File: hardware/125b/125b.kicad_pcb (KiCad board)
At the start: 2 copper layers, 59 x 75 mm, 52 parts, among them J1 Guitar in, J2 Barrel_Jack, J3 Conn_02x05_Odd_Even_MountingP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, J4 NRJ6HF, SW1 SW_DIP_x02, SW2 RotaryEncoder_Switch, SW3 Switch 1, SW4 Switch 2, U1 L78L05_TO92, U2 TL074

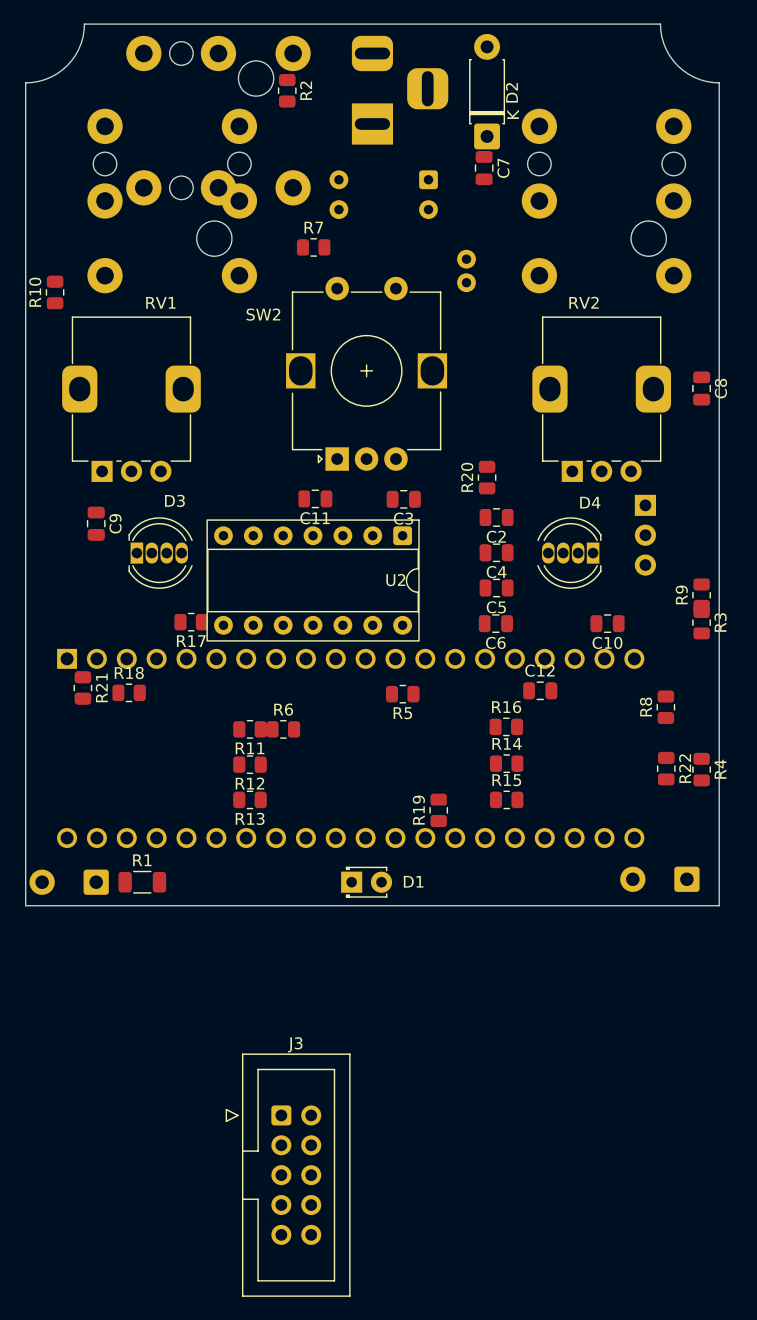
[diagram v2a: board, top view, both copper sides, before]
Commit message: Update 3d models and adjust footprints for local project lib
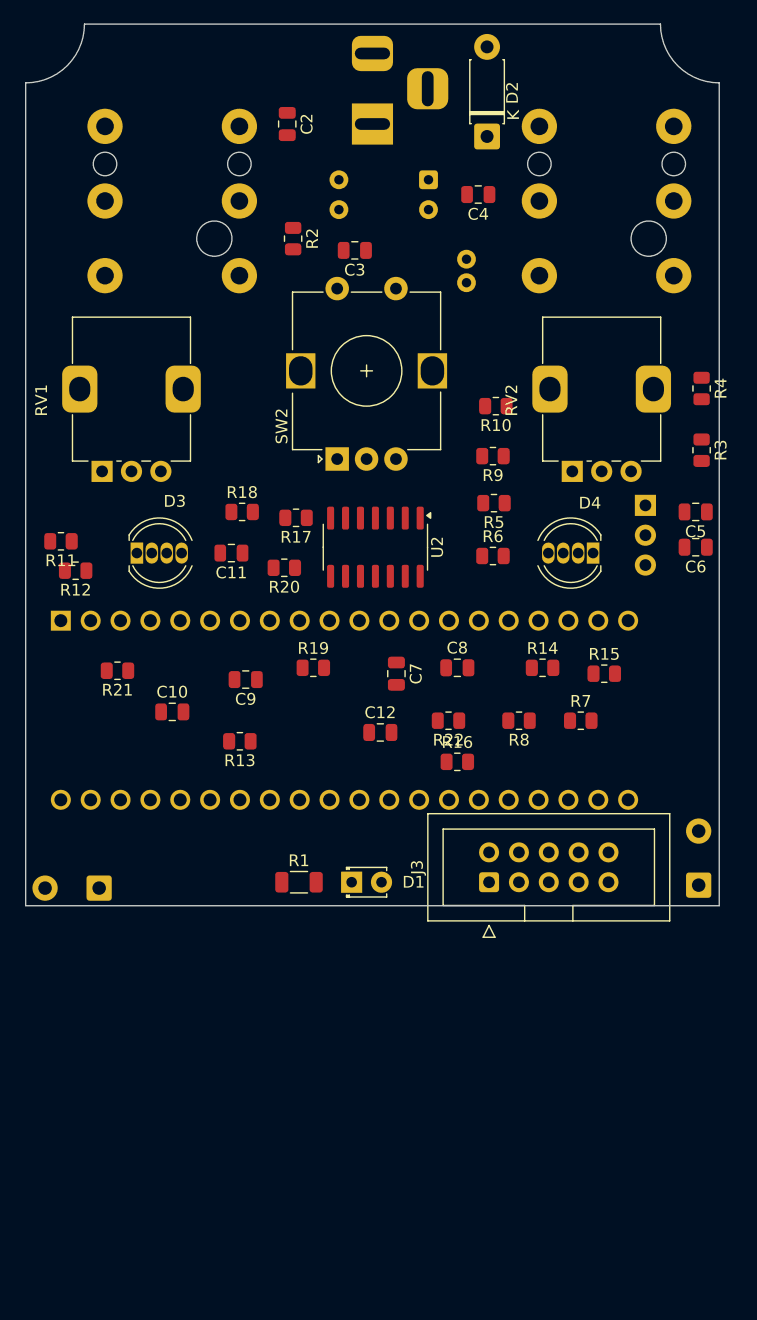
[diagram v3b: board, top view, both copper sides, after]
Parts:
- removed the J4 at (120.8, 37.5)
- A1: footprint Module:Electrosmith_Daisy_Seed -> Library:Electrosmith_Daisy_Seed
- J1: footprint Connector_Audio:Jack_6.35mm_Neutrik_NRJ6HF-1-AU_Horizontal -> Library:Jack_6.35mm_Neutrik_NRJ6HF-1-AU_Horizontal
- J4: value NRJ6HF -> Guitar out; footprint Connector_Audio:Jack_6.35mm_Neutrik_NRJ6HF_Horizontal -> Library:Jack_6.35mm_Neutrik_NRJ6HF-1-AU_Horizontal
- RV1, RV2: footprint Potentiometer_THT:Potentiometer_Alps_RK09K_Single_Vertical -> Project:Potentiometer_Alps_RK09K_Single_Vertical
- SW2: footprint Rotary_Encoder:RotaryEncoder_Alps_EC12E-Switch_Vertical_H20mm -> Project:RotaryEncoder_Alps_EC12E-Switch_Vertical_H20mm
- U2: footprint Package_DIP:DIP-14_W7.62mm_Socket -> Package_SO:SOIC-14_3.9x8.7mm_P1.27mm
- moved R7 46.2 mm to (145.2, 94.3)
- moved C7 43.7 mm to (129.5, 90.3)
- moved R10 38.7 mm to (138.0, 67.5), turned to 180 degrees
- moved C2 37.9 mm to (120.2, 43.5), turned to -90 degrees
- moved C10 37.8 mm to (110.5, 93.5), turned to 0 degrees
- moved R4 32.4 mm to (155.5, 66.0)
- moved C8 31.6 mm to (134.7, 89.8), turned to 0 degrees
- moved C4 30.5 mm to (136.5, 49.5)
- moved J3 26.6 mm to (137.4, 108.0), turned to 90 degrees
- moved R6 23.1 mm to (137.8, 80.2)
- moved R11 22.7 mm to (101.0, 79.0)
- moved R12 22.2 mm to (102.2, 81.5)
- moved C3 21.6 mm to (126.0, 54.2)
- moved R9 21.3 mm to (137.8, 71.8), turned to 180 degrees
- moved R22 19.0 mm to (134.0, 94.3), turned to 180 degrees
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
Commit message: Tidy up position of SMD components
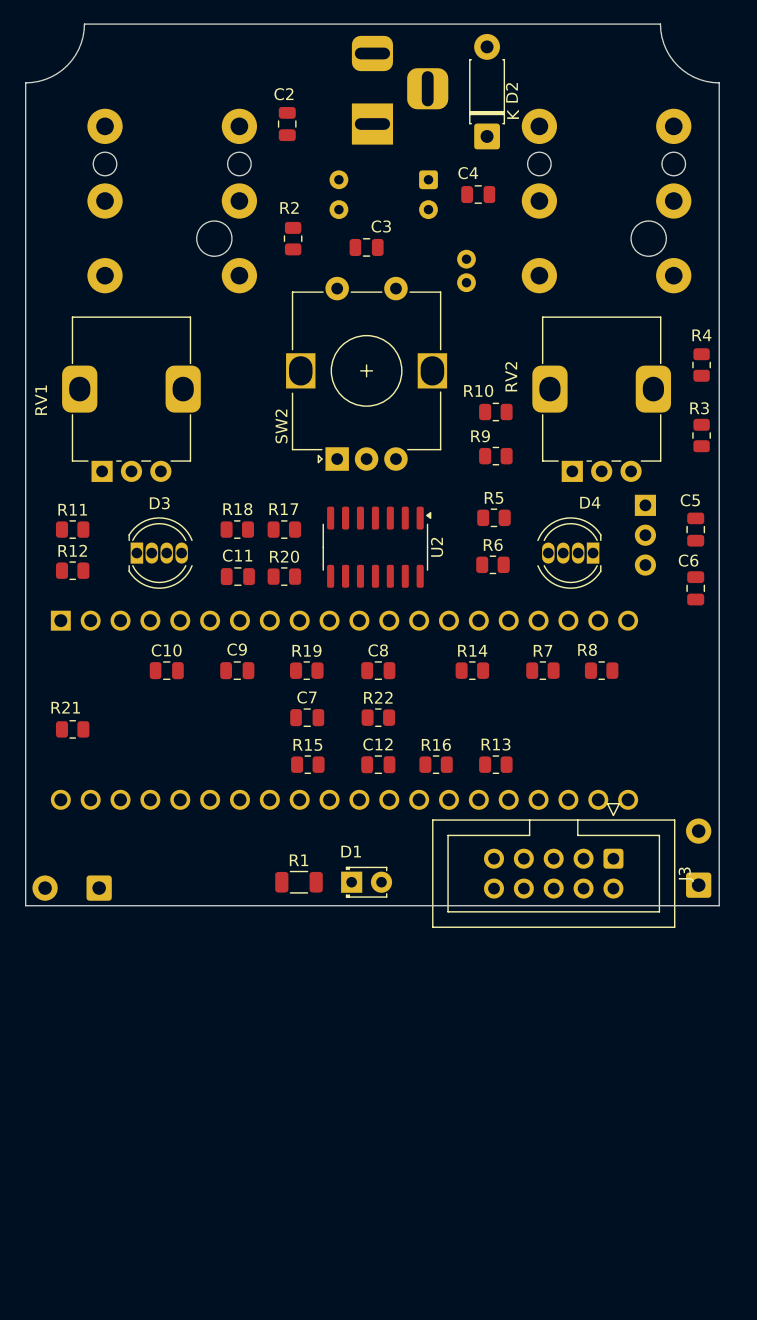
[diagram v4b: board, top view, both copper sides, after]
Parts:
- moved R15 26.4 mm to (122.0, 98.0)
- moved R13 21.9 mm to (138.0, 98.0)
- moved J3 10.8 mm to (148.0, 106.0), turned to -90 degrees
- moved C7 8.46 mm to (122.0, 94.0), turned to 0 degrees
- moved R8 8.22 mm to (147.0, 90.0)
- moved C8 6.72 mm to (128.0, 90.0)
- moved R21 6.28 mm to (102.0, 95.0)
- moved R22 5.98 mm to (128.0, 94.0), turned to 0 degrees
- moved R14 5.97 mm to (136.0, 90.0)
- moved R7 5.34 mm to (142.0, 90.0)
- moved C10 3.54 mm to (110.0, 90.0)
- moved C6 3.50 mm to (155.0, 83.0), turned to -90 degrees
- moved C12 2.75 mm to (128.0, 98.0)
- moved C11 2.07 mm to (116.0, 82.0)
- moved R4 2.00 mm to (155.5, 64.0), turned to 90 degrees
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
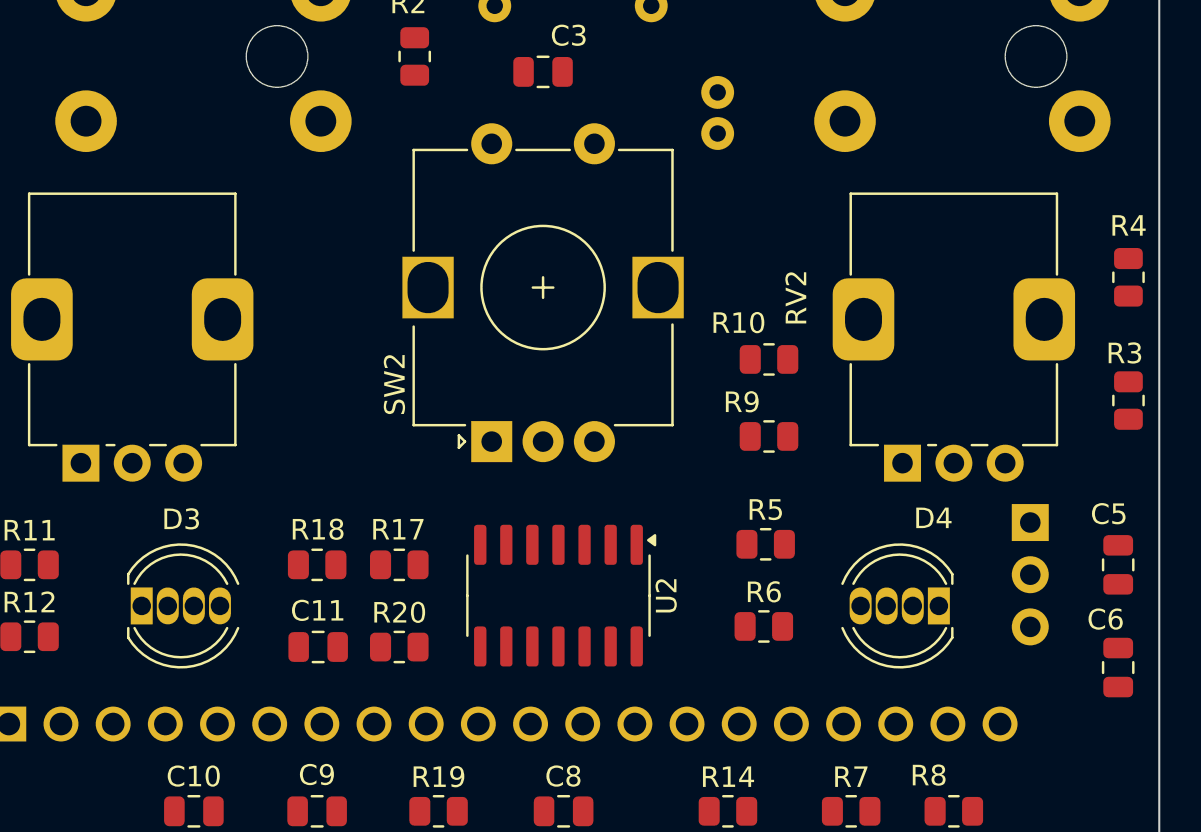
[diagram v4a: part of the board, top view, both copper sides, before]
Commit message: Increase RGB LED footprint for easier soldering
Also re-adjustLEDs, pots and encoder for symmetry
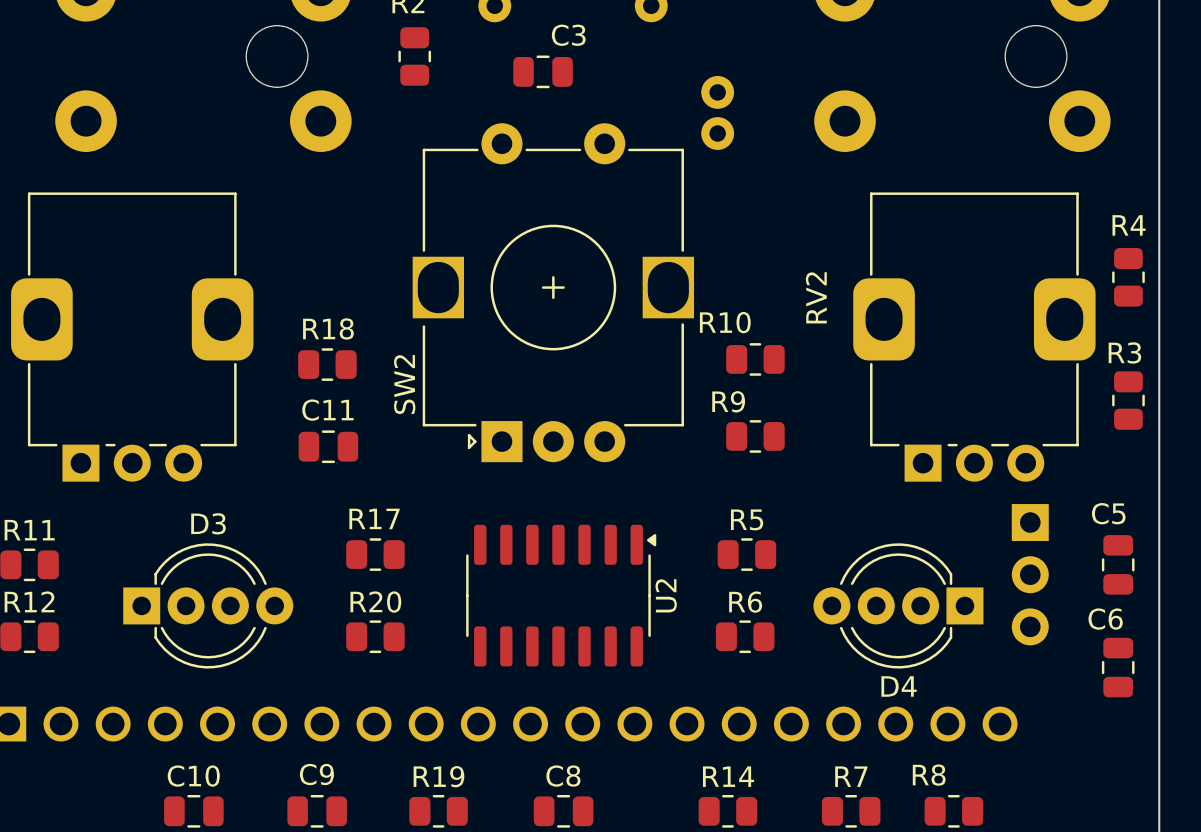
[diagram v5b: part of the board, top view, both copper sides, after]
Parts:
- D3, D4: footprint LED_THT:LED_D5.0mm-4_RGB -> LED_THT:LED_D5.0mm-4_RGB_Wide_Pins
- moved C11 9.76 mm to (116.5, 72.2)
- moved R18 9.76 mm to (116.5, 68.2)
- moved D4 1.27 mm to (147.5, 80.0)
- moved R17 1.27 mm to (118.8, 77.5)
- moved R20 1.27 mm to (118.8, 81.5)
- moved R5 1.04 mm to (136.9, 77.5)
- moved R6 1.04 mm to (136.8, 81.5)
- moved RV2 1.00 mm to (145.5, 73.0)
- moved R10 0.66 mm to (137.3, 68.0)
- moved R9 0.66 mm to (137.3, 71.8)
- moved SW2 0.50 mm to (125.0, 72.0)

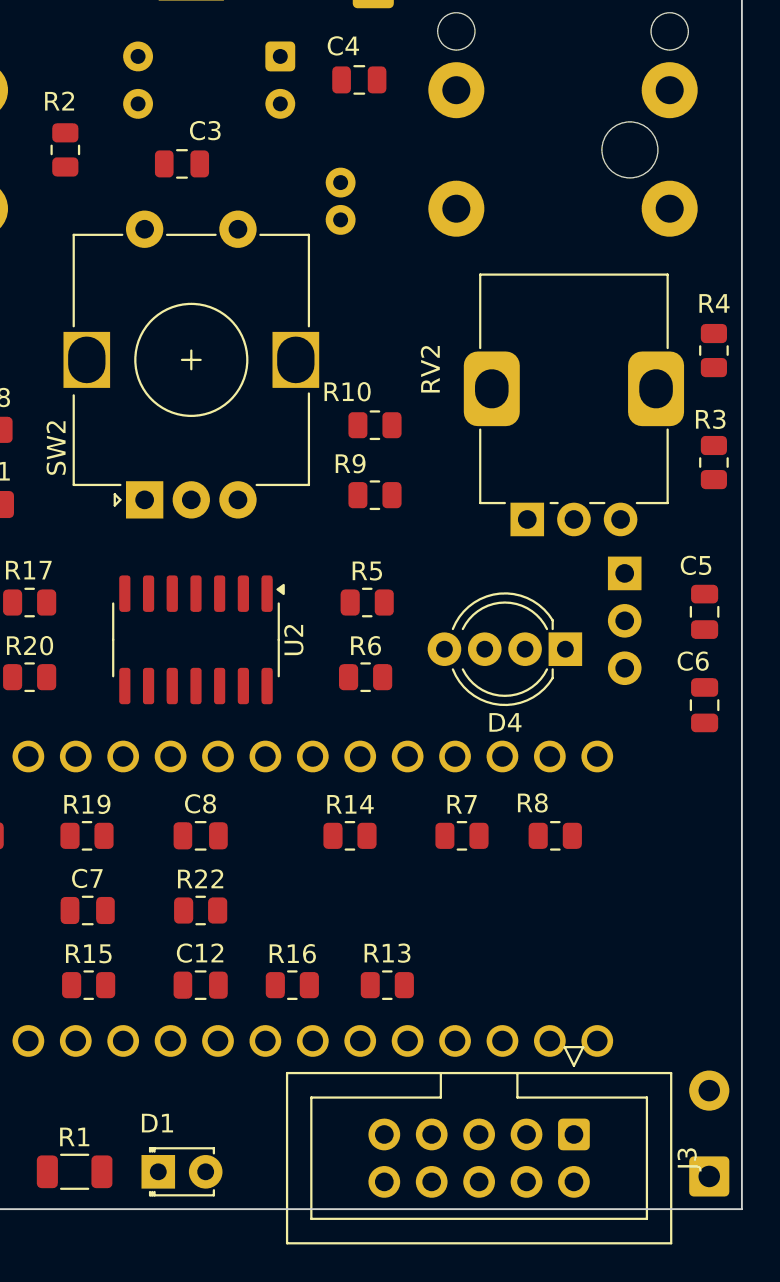
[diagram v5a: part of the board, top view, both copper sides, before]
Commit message: Try pin sockets for the footswitch connector
Can just solder some ribbon wire for this version
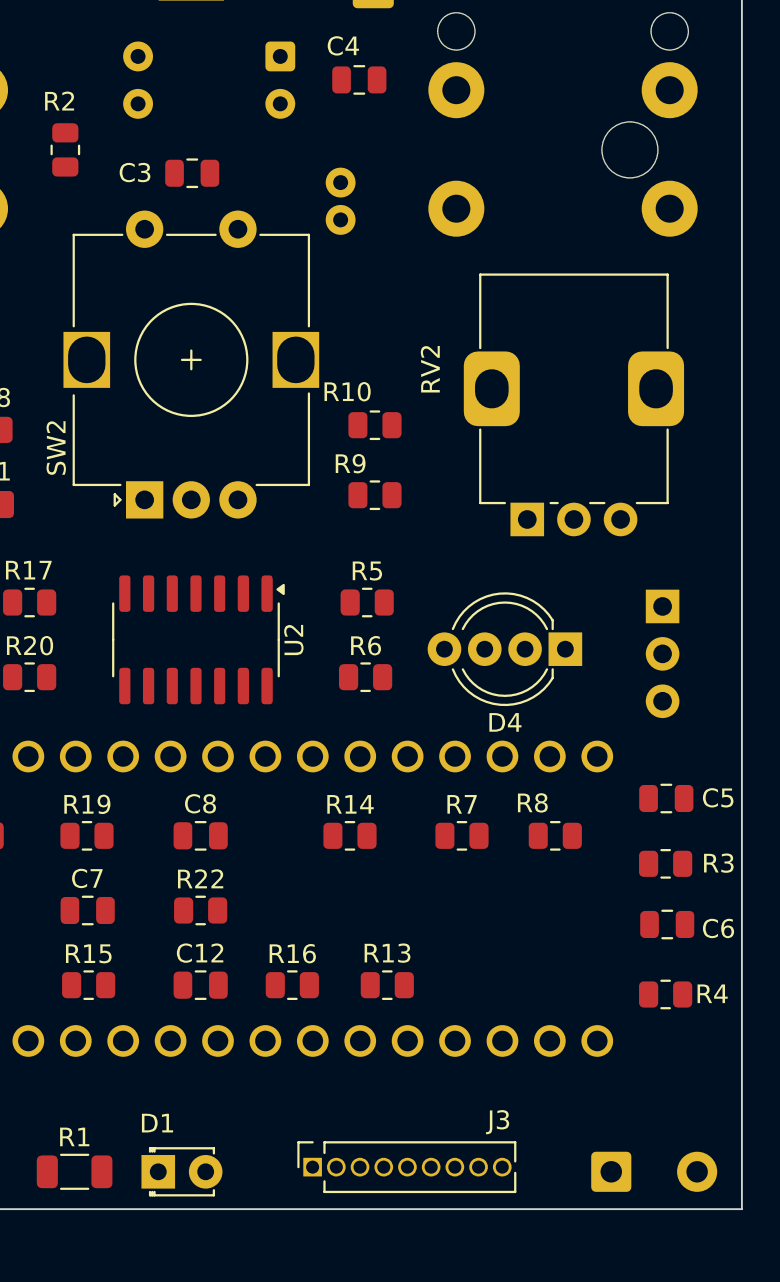
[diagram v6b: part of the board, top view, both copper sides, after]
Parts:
- J3: footprint Connector_IDC:IDC-Header_2x05_P2.54mm_Vertical -> Connector_PinSocket_1.27mm:PinSocket_1x09_P1.27mm_Vertical
- moved R4 34.6 mm to (152.9, 98.5), turned to 0 degrees
- moved R3 21.7 mm to (152.9, 91.5), turned to 180 degrees
- moved J3 14.1 mm to (134.0, 107.8), turned to 90 degrees
- moved C6 11.9 mm to (153.0, 94.8), turned to 180 degrees
- moved C5 10.2 mm to (152.9, 88.0), turned to 180 degrees
- moved SW4 5.26 mm to (150.0, 108.0), turned to 0 degrees
- moved U1 2.69 mm to (152.8, 77.7)
- moved C3 0.74 mm to (127.5, 54.5)

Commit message: Add GND plane zones
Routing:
- added copper zone on B.Cu, net GND
- added copper zone on F.Cu, net GND
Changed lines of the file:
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@@
+		)
+	)
+	(zone
+		(net 20)
+		(net_name "GND")
+		(layers "F.Cu" "B.Cu")
+		(hatch edge 0.5)
+		(connect_pads
+			(clearance 0.4)
+		)
+		(min_thickness 0.25)
+		(filled_areas_thickness no)
+		(fill
+			(thermal_gap 0.5)
+			(thermal_bridge_width 0.5)
+		)
+		(polygon
+			(pts
+				(xy 150 35.75) (xy 156.5 42.25) (xy 156.5 109.25) (xy 156.25 109.5) (xy 98.5 109.5) (xy 98.5 42)
+				(xy 104.75 35.75)
+			)
 		)
 	)

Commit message: Everything connected together
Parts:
- C5, R20, R5, R6, R9, U2: moved to B.Cu
- moved R3 65.6 mm to (109.8, 42.0)
- moved R4 60.2 mm to (121.0, 47.5), turned to 180 degrees
- moved C7 56.8 mm to (147.0, 43.0)
- moved A1 55.8 mm to (153.9, 103.2), turned to 90 degrees
- moved C8 44.5 mm to (146.9, 49.8), turned to 180 degrees
- moved R8 39.5 mm to (108.6, 99.0)
- moved R21 30.0 mm to (116.5, 68.8), turned to 0 degrees
- moved R7 29.5 mm to (114.0, 99.2)
- moved R17 28.2 mm to (110.0, 50.8)
- moved C5 26.3 mm to (138.4, 66.0), turned to -90 degrees
- moved R13 26.1 mm to (115.3, 85.0)
- moved R10 23.8 mm to (146.9, 46.2), turned to 180 degrees
- moved R15 23.4 mm to (141.4, 85.0)
- moved R18 22.7 mm to (109.9, 46.5)
- moved R5 16.0 mm to (120.9, 76.6), turned to 0 degrees
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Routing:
- net Net-(D2-A): track 0.00 -> 123.6 mm, vias 0 -> 2
- net +5V: track 0.00 -> 110.9 mm, vias 0 -> 3
- net /fsw6: track 0.00 -> 100.0 mm, vias 0 -> 1
- net Net-(C7-Pad2): track 0.00 -> 95.1 mm, vias 0 -> 2
- net /fsw7: track 0.00 -> 92.3 mm
- net /VCC: track 0.00 -> 76.5 mm
- net Net-(U2C-+): track 0.00 -> 75.0 mm, vias 0 -> 2
- net /3v3: track 0.00 -> 68.0 mm
- net /fsw4: track 0.00 -> 66.8 mm
- net Net-(U2B-+): track 0.00 -> 66.7 mm, vias 0 -> 1
- net Net-(U2A-+): track 0.00 -> 65.7 mm
- net /fsw3: track 0.00 -> 63.1 mm, vias 0 -> 3
- net /ENC_CLICK: track 0.00 -> 59.0 mm, vias 0 -> 2
- net Net-(A1-SAI2_FS): track 0.00 -> 53.4 mm, vias 0 -> 1
- net Net-(A1-ADC_0): track 0.00 -> 46.7 mm
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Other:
- board text added: "Crouds v0.5 Denis Crowdy, Prog Pedals"
- board text removed: "Podal v0.4 Denis Crowdy"
